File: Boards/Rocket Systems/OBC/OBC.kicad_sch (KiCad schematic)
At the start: 66 parts, among them IC1 NEO-M8Q-0, IC2 NSVT30010MXV6T1G, IC3 BC846BLT1G, J1 22027063, J3 SMARA_CONNECTOR, J4 5023520200, Q1 BC857CMB_315, U12 BMI323, U4 LPS22DFTR, U6 VLMKG3400-GS08, U7 BMP581, U8 LSM6DSOTR, U9 LIS2MDLTR

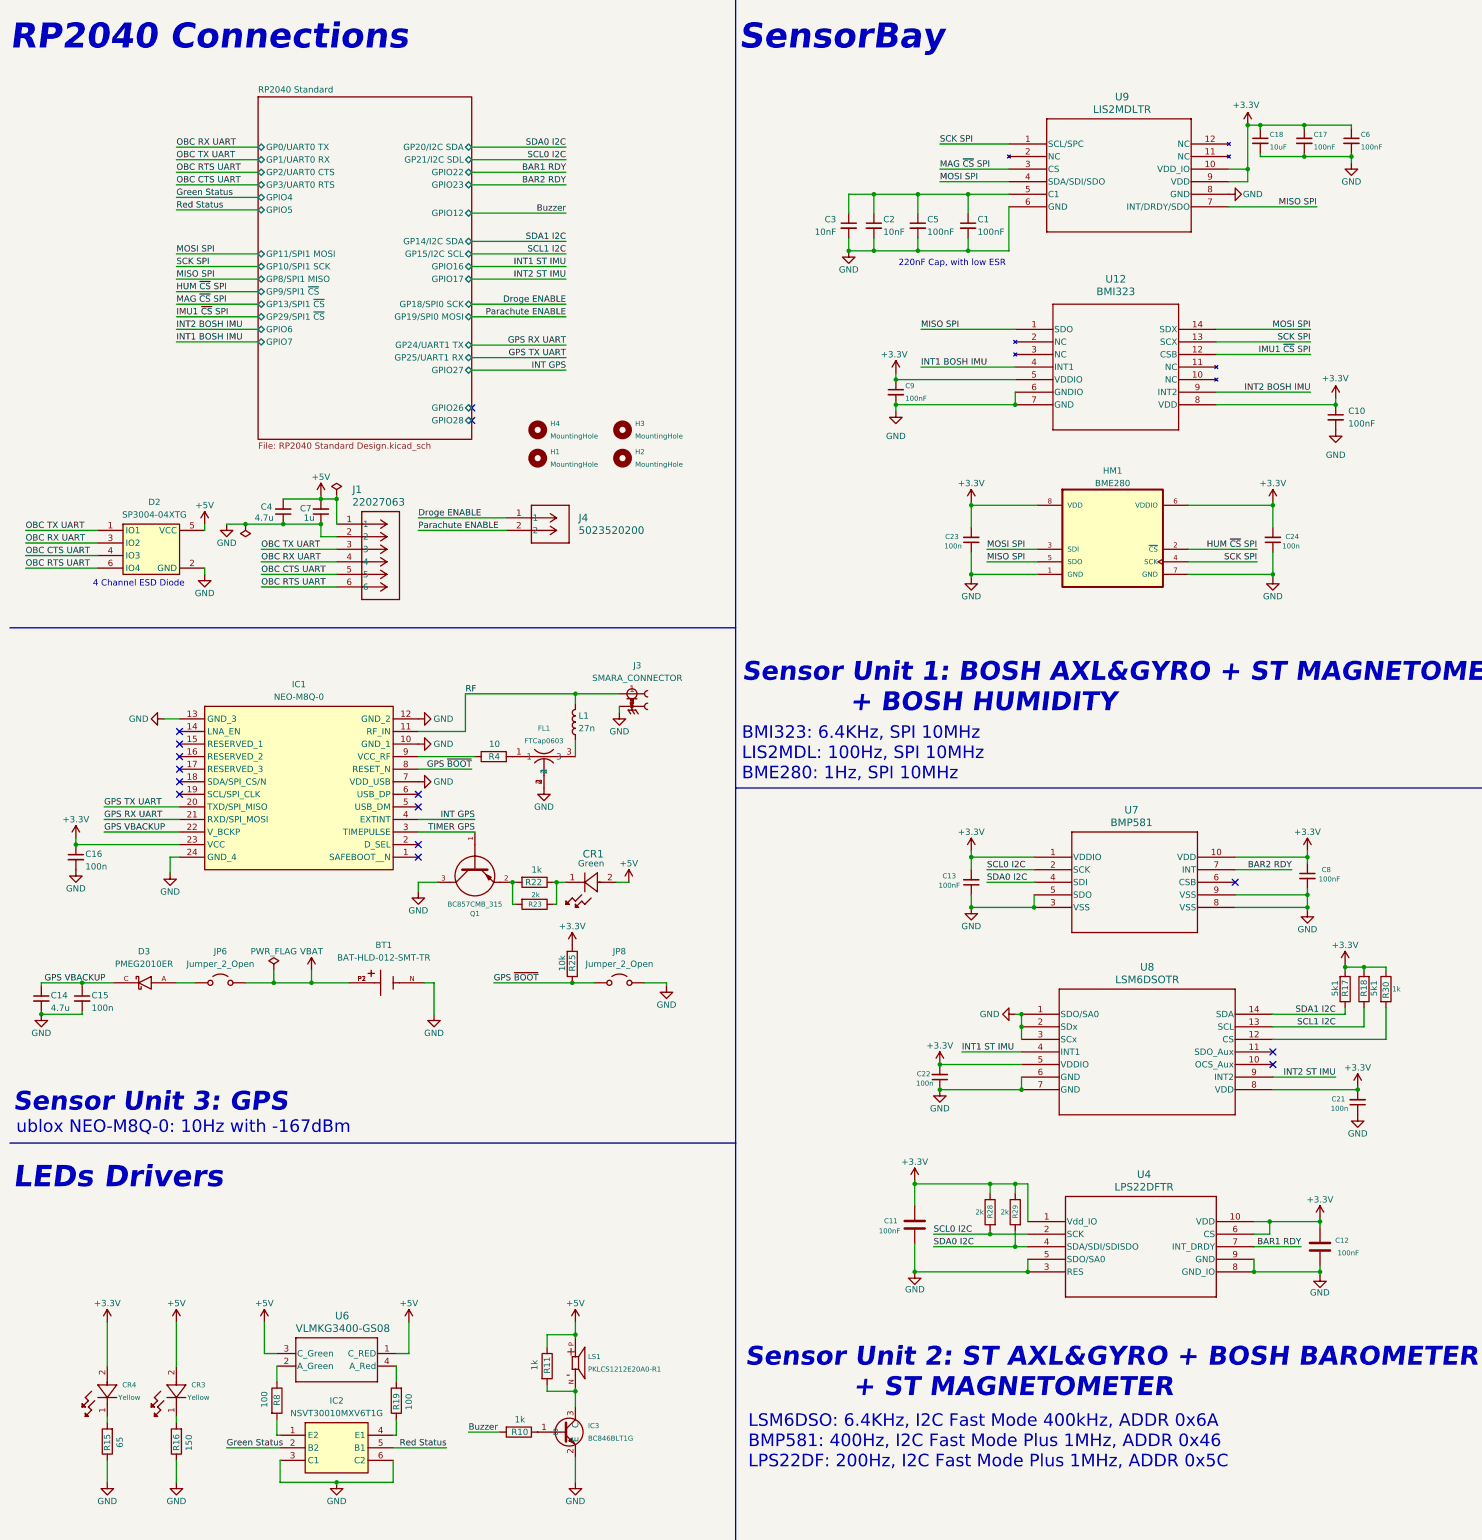
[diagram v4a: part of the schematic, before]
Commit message: OBC a Navigator Updates
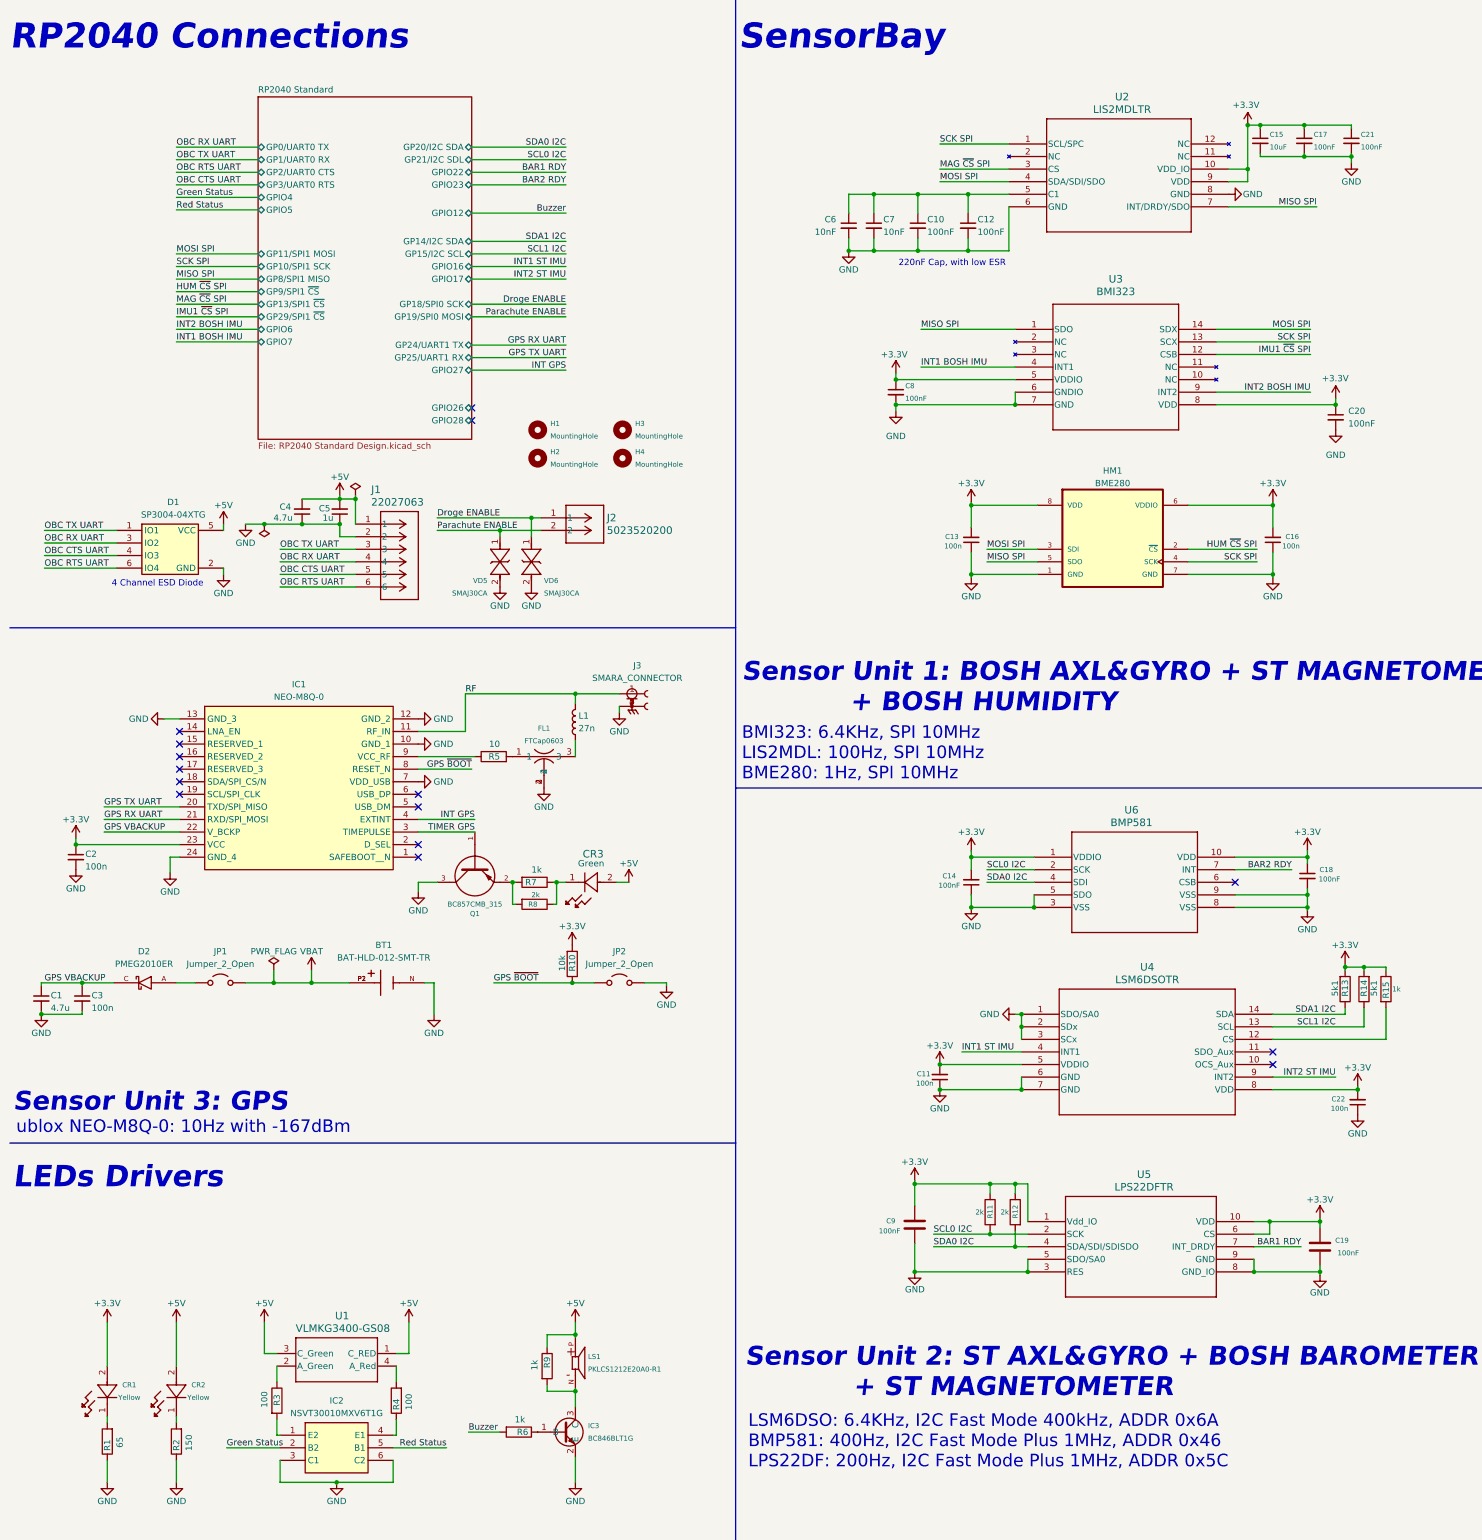
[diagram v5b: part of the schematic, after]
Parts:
- added VD5, VD6: SMAJ30CA, SMAJ30CA:SMASeries_LTF, symbol SMAJ30CA:SMAJ30CA
- renumbered C14 to C1, C5 to C10, C22 to C11, C1 to C12, C23 to C13, C13 to C14, C18 to C15, C24 to C16, C8 to C18, C12 to C19, C16 to C2, C10 to C20, C6 to C21, C21 to C22, C15 to C3, C7 to C5, C3 to C6, C2 to C7, C9 to C8, C11 to C9, CR4 to CR1, CR3 to CR2, CR1 to CR3, D2 to D1, D3 to D2, H4 to H1, H1 to H2, H2 to H4, J4 to J2, JP6 to JP1, JP8 to JP2, R15 to R1, R25 to R10, R28 to R11, R29 to R12, R17 to R13, R18 to R14, R30 to R15, R16 to R2, R8 to R3, R19 to R4, R4 to R5, R10 to R6, R22 to R7, R23 to R8, R11 to R9, U6 to U1, U9 to U2, U12 to U3, U8 to U4, U4 to U5, U7 to U6
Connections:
- net Droge ENABLE: now also VD6.1
- net GND: now also VD5.2, VD6.2
- net Parachute ENABLE: now also VD5.1
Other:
- moved on the sheet: C4, C5, D1, J1, J2

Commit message: Repo rename and update
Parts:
- removed BT1: BAT-HLD-012-SMT-TR, BAT_HLD_012:BAT_BAT-HLD-012-SMT-TR, symbol BAT-HLD-012-SMT-TR:BAT-HLD-012-SMT-TR
- removed C1: 4.7u, Capacitor-0402:Capacitor_0402, symbol Device:C_Small
- removed C10, C14, C21, C8: 100nF, Capacitor-0402:Capacitor_0402, symbol Device:C_Small
- removed C11, C13, C22, C3: 100n, Capacitor-0402:Capacitor_0402, symbol Device:C_Small
- removed C5: 1u, Capacitor-0402:Capacitor_0402, symbol Device:C_Small
- removed C7: 10nF, Capacitor-0402:Capacitor_0402, symbol Device:C_Small
- removed CR3: VLMC3100-GS08, LED-Green_VLMC3100-GS08:LED_PLCC_VSMB, symbol GreenLED__VLMC3100-GS08:VLMC3100-GS08
- removed D2: PMEG2010ER, Diode-Schottky_PMEG2010ER:SODFL3517X110N, symbol PMEG2010ER:PMEG2010ER
- removed FL1: FTCap0603, FTCap_0603:FTCap_0603, symbol FTCap0603:FTCap0603
- removed HM1: BME280, BME280:BME280, symbol BME280:BME280
- removed IC1: NEO-M8Q-0, NEO-M8Q-0:NEO-M8_UBL, symbol NEO-M8Q-0:NEO-M8Q-0
- removed IC2: NSVT30010MXV6T1G, 2 PNP:SOT-563_1P3X1P7_ONS, symbol NSVT30010MXV6T1G:NSVT30010MXV6T1G
- removed IC3: BC846BLT1G, BJT NPN:SOT96P237X111-3N, symbol BC846BLT1G:BC846BLT1G
- removed J1: 22027063, 6 Female Conn:CONN6X1_22027063_MOL, symbol 022027063:22027063
- removed J3: SMARA_CONNECTOR, Side Angle SMA:SMARACONNECTOR, symbol SMARA_CONNECTOR:SMARA_CONNECTOR
- removed JP2: Jumper_2_Open, Jumper:SolderJumper-2_P1.3mm_Open_RoundedPad1.0x1.5mm, symbol Jumper:Jumper_2_Open
- removed Q1: BC857CMB_315, PNP_BC857CMB_315:TRANS_PMZB550UNEYL, symbol BC857CMB_315:BC857CMB_315
- removed R15: 1k, Resistor-0402:RES_0402, symbol Device:R
- removed U1: VLMKG3400-GS08, VLMKG3400-GS08:SMT_00-GS08_VIS, symbol VLMKG3400-GS08:VLMKG3400-GS08
- removed U2: LIS2MDLTR, MAG LIS2MDLTR:LGA-12_2X2X1_STM, symbol MAG_LIS2MDLTR:LIS2MDLTR
- removed U3: BMI323, IMU BMI323:BMI323_BOS, symbol IMU_BMI323:BMI323
- removed U4: LSM6DSOTR, LSM6DSOTR:LGA-14L_2P5X3X0P86_STM, symbol LSM6DSOTR:LSM6DSOTR
- removed U5: LPS22DFTR, BARO LPS22DFTR:QFN_22DFTR_STM, symbol BARO_LPS22DFTR:LPS22DFTR
- removed U6: BMP581, BARO BMP581:QFN10_BMP581_BOS, symbol BARO_BMP581:BMP581
- removed VD5, VD6: SMAJ30CA, SMAJ30CA:SMASeries_LTF, symbol SMAJ30CA:SMAJ30CA
- added C1, C3: 10nF, Capacitor-0402:Capacitor_0402, symbol Device:C
- added C10, C5: 100nF, Capacitor-0402:Capacitor_0402, symbol Device:C
- added C11, C14: 1.2pF, Capacitor-0402:Capacitor_0402, symbol Device:C
- added C13: 0.5pF, Capacitor-0402:Capacitor_0402, symbol Device:C
- added C21: 0.3p, Capacitor-0402:Capacitor_0402, symbol Device:C
- added C7: 470nF, Capacitor-0402:Capacitor_0402, symbol Device:C
- added C8: 0.8pF, Capacitor-0402:Capacitor_0402, symbol Device:C
- added D2: SP3004-04XTG, TVS-SP3004:SOT563_LTF, symbol SP3004-04XTG:SP3004-04XTG
- added IC1: NSVT30010MXV6T1G, 2 PNP:SOT-563_1P3X1P7_ONS, symbol NSVT30010MXV6T1G:NSVT30010MXV6T1G
- added IC2: BC846BLT1G, BJT NPN:SOT96P237X111-3N, symbol BC846BLT1G:BC846BLT1G
- added J1: 1718560006, 6 Male Conn:CONN06_1718560006_MOL, symbol 1718560006:1718560006
- added J3: MEM2061-01-188-00-A_REVA, SD-CARD_MEM2061-01-188-00-A:GCT_MEM2061-01-188-00-A_REVA, symbol MEM2061-01-188-00-A_REVA:MEM2061-01-188-00-A_REVA
- added J4: SMARA_CONNECTOR, Side Angle SMA:SMARACONNECTOR, symbol SMARA_CONNECTOR:SMARA_CONNECTOR
- added L2: 3nH, Inductor-0402:Inductor_0402, symbol Device:L
- added L3: 2.5nH, Inductor-0402:Inductor_0402, symbol Device:L
- added L4: 1.9nH, Inductor-0201:Inductor_0201, symbol Device:L
- added MP1, MP2, MP3, MP4: S0991-46R, S0991-46R:S099146R, symbol S0991-46R:S0991-46R
- added U1: SX1280IMLTRT, SX1280:QFN24_4X4_SEM, symbol SX1280:SX1280IMLTRT
- added U2: STLM20DD9F, STLM20DD9F:UDFN-4L_STM, symbol STLM20DD9F:STLM20DD9F
- added U3: NRF21540-QDAA-R, RF FEM:QFN16_4X4_NOR, symbol NRF21540-QDAA-R:NRF21540-QDAA-R
- added U4: THVD2410VDRCR, THVD2410VDRCR:VSON10_DRC_TEX, symbol THVD2410VDRCR:THVD2410VDRCR
- added U5: VLMKG3400-GS08, VLMKG3400-GS08:SMT_00-GS08_VIS, symbol VLMKG3400-GS08:VLMKG3400-GS08
- added VD1, VD2: SMAJ30CA, SMAJ30CA:SMASeries_LTF, symbol SMAJ30CA:SMAJ30CA
- added XTAL1: NX2016SA-52MHZ-EXS00A-CS07103, NX2016SA_52MHZ:OSCCC200X160X50N, symbol NX2016SA-52MHZ-EXS00A-CS07103:NX2016SA-52MHZ-EXS00A-CS07103
- C12: value 100nF -> 10u; footprint Capacitor-0402:Capacitor_0402 -> Capacitor-0805:Capacitor_0805
- C15: value 10uF -> 1p; footprint Capacitor-0805:Capacitor_0805 -> Capacitor-0402:Capacitor_0402
- C17, C18, C20: value 100nF -> 100n
- C19: value 100nF -> 0.9p
- C2: value 100n -> 4.7u
- C4: value 4.7u -> 1u
- C6: value 10nF -> 100n
- L1: value 27n -> 15uH; footprint Inductor-0402:Inductor_0402 -> Inductor-0805:Inductor_0805
- R1: value 65 -> 1k
- R10: value 10k -> 523
- R11: value 2k -> 120; footprint Resistor-0402:RES_0402 -> Resistor-0603:RES_0603
- R12: value 2k -> 523
- R13: value 5k1 -> 65
- R14: value 5k1 -> 150
- R2: value 150 -> 10k
- R3: value 100 -> 10k
- R5: value 10 -> 100
- R8: value 2k -> 0; now not fitted; now left out of the parts list
- R9: value 1k -> 0
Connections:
- net GPS ~{BOOT} is gone; now on net +5V: R10.1
- net SCL0 I2C is gone; now on net RS_DP: R11.2
- net SCL1 I2C is gone; now on net GND: R14.1
- net SDA0 I2C is gone; now on net GND: R12.2
- net SDA1 I2C is gone; now on net GND: R13.1
- net +3.3V: now also C12.1, C9.1, R2.1, C10.1, C5.1, D2.5 (VCC), J3.4 (VDD), U1.11 (VBAT_IO), U1.15 (VBAT), U2.4 (VCC), U3.5 (VDD), U3.6 (VDD), U4.1 (VIO); no longer C15.1, C19.2, C2.1, C20.1, C9.2, R10.2, R11.1, R12.1, R13.2, R14.2
- net +5V: now also C2.2, C20.1, C6.2, R7.1, R8.2, J1.1, U4.10 (VCC), U5.1 (C_RED), U5.3 (C_Green); no longer R9.1
- net GND: now also C19.2, C2.1, C6.1, C9.2, JP1.1 (A), R3.2, R9.2, C1.2, C10.2, C11.2, C14.2, C21.2, C3.2, C5.2, C7.2, C8.2, D2.2 (GND), IC1.3 (C1), IC1.6 (C2), IC2.2 (E), J1.2, J3.10 (CD2), J3.11 (GND), J3.12 (GND), J3.6 (VSS), J3.9 (CD1), J4.2, J4.3, J4.4, J4.5, MP1.1, MP1.2, MP1.3, MP2.1, MP2.2, MP2.3, MP3.1, MP3.2, MP3.3, MP4.1, MP4.2, MP4.3, U1.13 (GND), U1.20 (GND), U1.21 (GND), U1.23 (GND), U1.24 (GND), U1.25 (GND), U1.5 (GND), U2.3 (GND), U3.1 (VSS), U3.16 (VSS), U3.17 (VSS), U3.8 (ANT_SEL), U4.11 (EPAD), U4.6 (GND), VD1.2, VD2.2, XTAL1.2 (GND), XTAL1.4 (GND__1); no longer C15.2, C19.1, C2.2, C6.2, C9.1, R1.1, R2.1
- net Green Status: now also IC1.2 (B2)
- net Red Status: now also IC1.5 (B1)
- net ENABLE_RS: now reaches R3.1
- net ENABLE_RS: now also U4.3 (DE), U4.4 (~{RE})
- net at R4.2: now also IC1.1 (E2)
- net at LS1.N: now also R7.2, IC2.3 (C); no longer R9.2
- net at R6.1: now also IC2.1 (B)
- net at CR1.1: now also R13.2; no longer R1.2
- net at R8.1: now also R9.1, U4.7 (SLR); no longer R7.1
- net at R5.2: now also U5.4 (A_Red)
- net at L1.1: now also C3.1, C7.1, U1.12 (DCC_FB), U1.2 (VDD_INN)
- net at R4.1: now also U5.2 (A_Green)
- net at R5.1: now also IC1.4 (E1)
- net at CR2.1: now also R14.2; no longer R2.2
- net Droge ENABLE renamed RS_DN
- net RS_DN: now also R10.2, R11.1, U4.9 (B), VD2.1
- net OBC CTS UART renamed Nav RTS UART
- net Nav RTS UART: now also J1.5
- net OBC RTS UART renamed Nav CTS UART
- net Nav CTS UART: now also J1.6
- net OBC RX UART renamed Nav TX UART
- net Nav TX UART: now also J1.4
- net OBC TX UART renamed Nav RX UART
- net Nav RX UART: now also J1.3
- net Parachute ENABLE renamed RS_DP
- net RS_DP: now also R12.1, U4.8 (A), VD1.1
- net RF: no longer names the net of L1.2
- net RF: now also U1.14 (DCC_SW)
- net VBAT: no longer names the net of JP1.2 (B)
- net VBAT: now also R1.1
- new net: C1.1, U1.1 (VR_PA)
- new net: C8.1, L2.1, U1.22 (RFIO)
- new net: C11.1, C13.2, L2.2, L3.1
- new net: C13.1, C14.1, C15.1, L3.2
- new net: C19.1, C21.1, J4.1, L4.2
- new net: C15.2, U3.10 (TRX)
- new net: L4.1, U3.2 (ANT1)
- new net BUSY SX1280: U1.7 (BUSY)
- new net DIO1 SX1280: U1.8 (DIO1)
- new net DIO2 SX1280: U1.9 (DIO2)
- new net DIO3 SX1280: U1.10 (DIO3)
- new net MODE NRF21540: U3.4 (MODE)
- new net NRF21540 ~{CS} SPI: U3.15 (CSN)
- new net RADIO MISO SPI: U1.16 (MISO_TX), U3.14 (MISO)
- new net RADIO MOSI SPI: U1.17 (MOSI_RX), U3.13 (MOSI)
- new net RADIO SCK SPI: U1.18 (SCK_RTSN), U3.12 (SCK)
- new net READ_RS: R2.2, U4.2 (R)
- new net RX_EN NRF21540: U3.7 (RX_EN)
- new net SD-Card  ~{CS} SPI: D2.3 (IO2), J3.2 (CD/DAT3)
- new net SD-Card MISO SPI: D2.1 (IO1), J3.7 (DAT0)
- new net SD-Card MOSI SPI: D2.4 (IO3), J3.3 (CMD)
- new net SD-Card SCK SPI: D2.6 (IO4), J3.5 (CLK)
- new net SX1280 XTA -: U1.4 (XTA), XTAL1.3
- new net SX1280 XTB +: U1.6 (XTB), XTAL1.1
- new net SX1280 ~{CS} SPI: U1.19 (NSS_CTS)
- new net TX_EN NRF21540: U3.9 (TX_EN)
- new net Temp_Sense: U2.1 (VOUT)
- new net WRITE_RS: U4.5 (D)
- new net ~{PDN} NRF21540: U3.11 (PDN)
- new net ~{RST} SX1280: R1.2, U1.3 (NRESET)
- no-connect marks 15 -> 4
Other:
- removed sheet RP2040 Standard
- added sheet RP2040 (RP2040 Standard Design.kicad_sch)
- note added: "16G SD-Card"
- note added: "FILTRO AQUI!!"
- note added: "LED & Buzzer Drivers"
- note added: "RF Front End Module"
- note added: "RFI Shield Clips"
- note added: "RS Transceiver (MASTER)"
- note added: "SLR LOW = 1Mpbs SLR HIGH = 250kbps"
- note added: "SPI must be limited to 5MHz"
- note added: "SX1280 2.4GHz LoRa & GFSK Transceiver"
- note added: "Temperature Sensor"
- note removed: "220nF Cap, with low ESR"
- note removed: "BMI323: 6.4KHz, SPI 10MHz LIS2MDL: 100Hz, SPI 10MHz BME280: 1Hz, SPI 10MHz"
- note removed: "LEDs Drivers"
- note removed: "LSM6DSO: 6.4KHz, I2C Fast Mode 400kHz, ADDR 0x6A BMP581: 400Hz, I2C Fast Mode Plus 1MHz, ADDR 0x46 LPS22DF: 200Hz, I2C Fast Mode Plus 1MHz, ADDR 0x5C"
- note removed: "Sensor Unit 1: BOSH AXL&GYRO + ST MAGNETOMETER + BOSH HUMIDITY"
- note removed: "Sensor Unit 2: ST AXL&GYRO + BOSH BAROMETER + ST MAGNETOMETER"
- note removed: "Sensor Unit 3: GPS"
- note removed: "SensorBay"
- note removed: "ublox NEO-M8Q-0: 10Hz with -167dBm"
- title: Navigator -> On Board Computer
- moved on the sheet: H1, H2, H3, H4, LS1

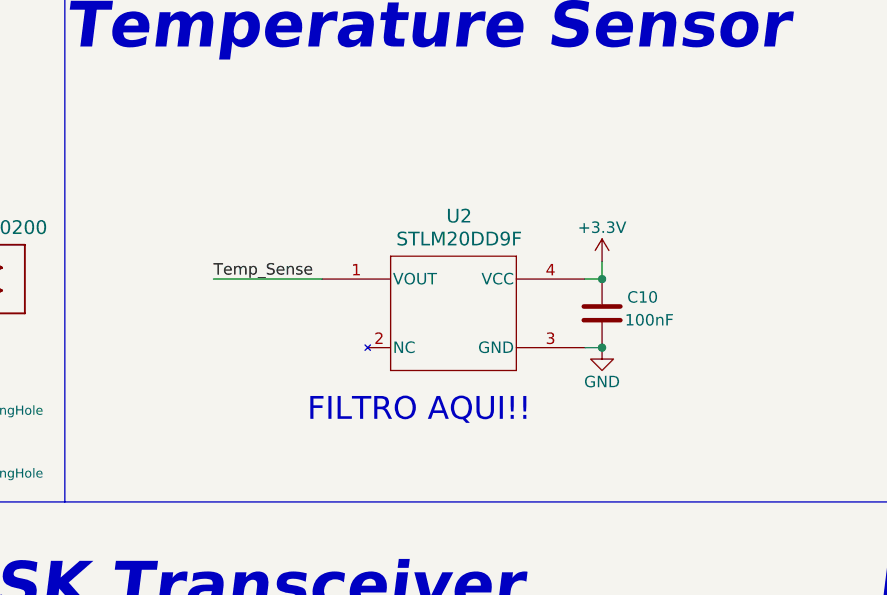
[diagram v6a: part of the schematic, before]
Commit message: temp sensor filter
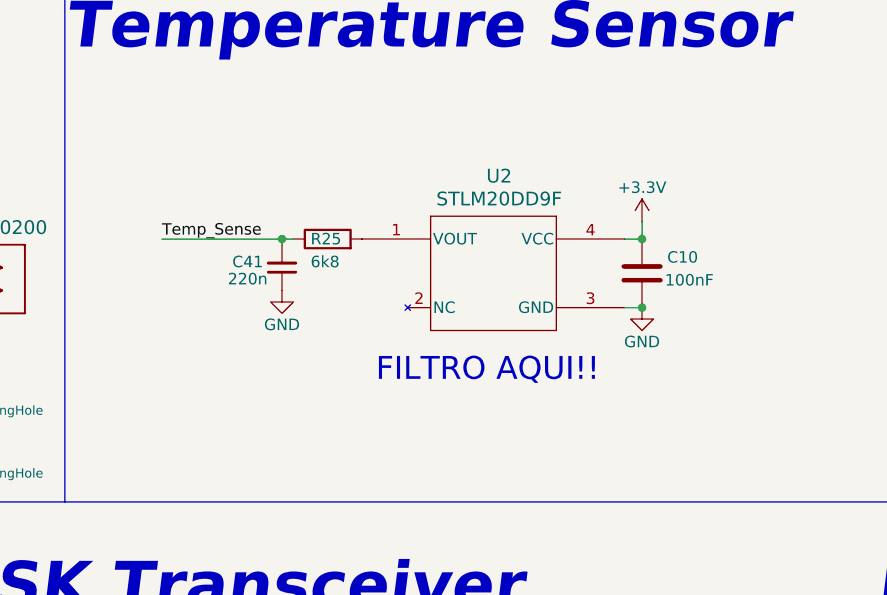
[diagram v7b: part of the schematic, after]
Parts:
- added C41: 220n, Capacitor-0402:Capacitor_0402, symbol Device:C_Small
- added R25: 6k8, Resistor-0402:RES_0402, symbol Device:R
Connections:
- net GND: now also C41.1
- net Temp_Sense: now also C41.2, R25.1; no longer U2.1 (VOUT)
- new net: R25.2, U2.1 (VOUT)
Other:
- moved on the sheet: C10, U2

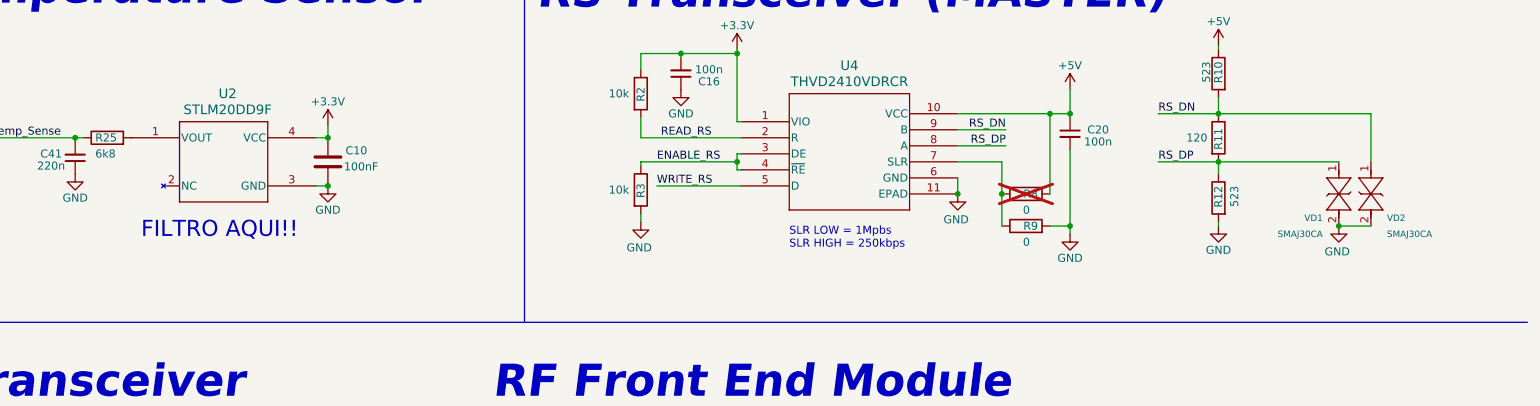
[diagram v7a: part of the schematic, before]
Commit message: ESD diodes and pinout update
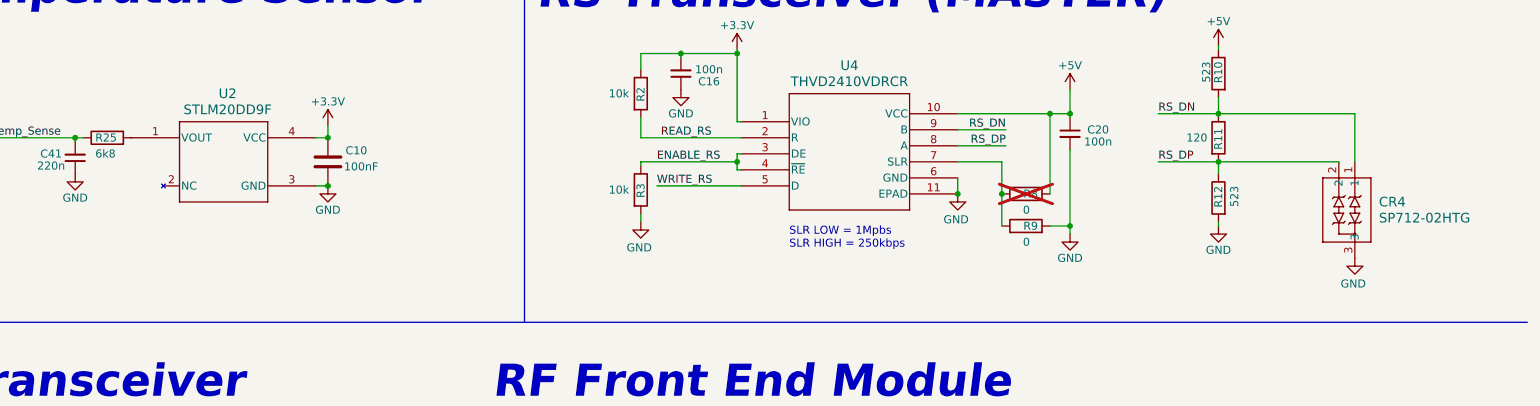
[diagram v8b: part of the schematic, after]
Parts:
- removed VD1, VD2: SMAJ30CA, SMAJ30CA:SMASeries_LTF, symbol SMAJ30CA:SMAJ30CA
- added CR4: SP712-02HTG, 2Channel ESD RS485 - P712-02HTG:SOT23-3_LTF, symbol SP712-02HTG:SP712-02HTG
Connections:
- net GND: now also CR4.3
- net RS_DN: now also CR4.1
- net RS_DP: now also CR4.2
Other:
- note removed: "FILTRO AQUI!!"
